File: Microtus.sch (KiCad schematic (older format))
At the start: 9 parts

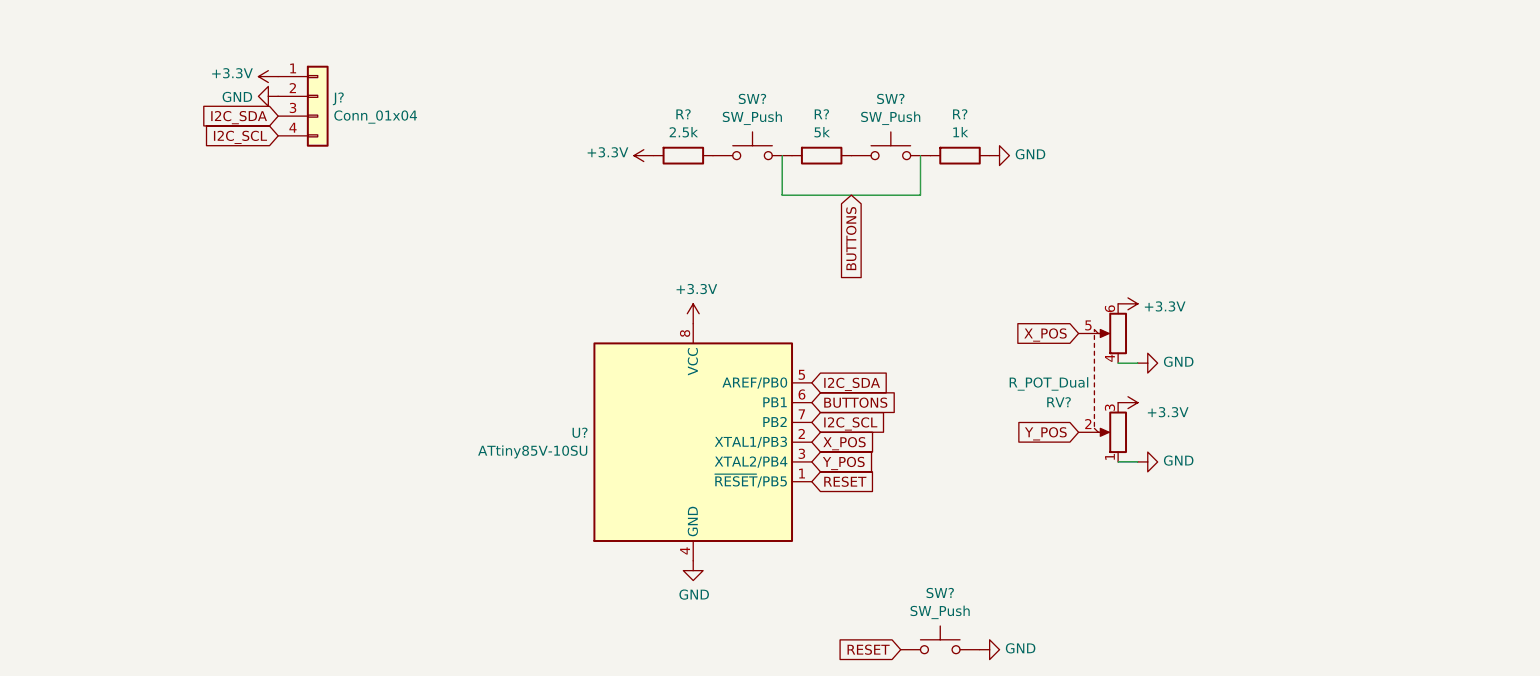
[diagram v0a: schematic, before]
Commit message: go with choc switches and 0805 SMDs
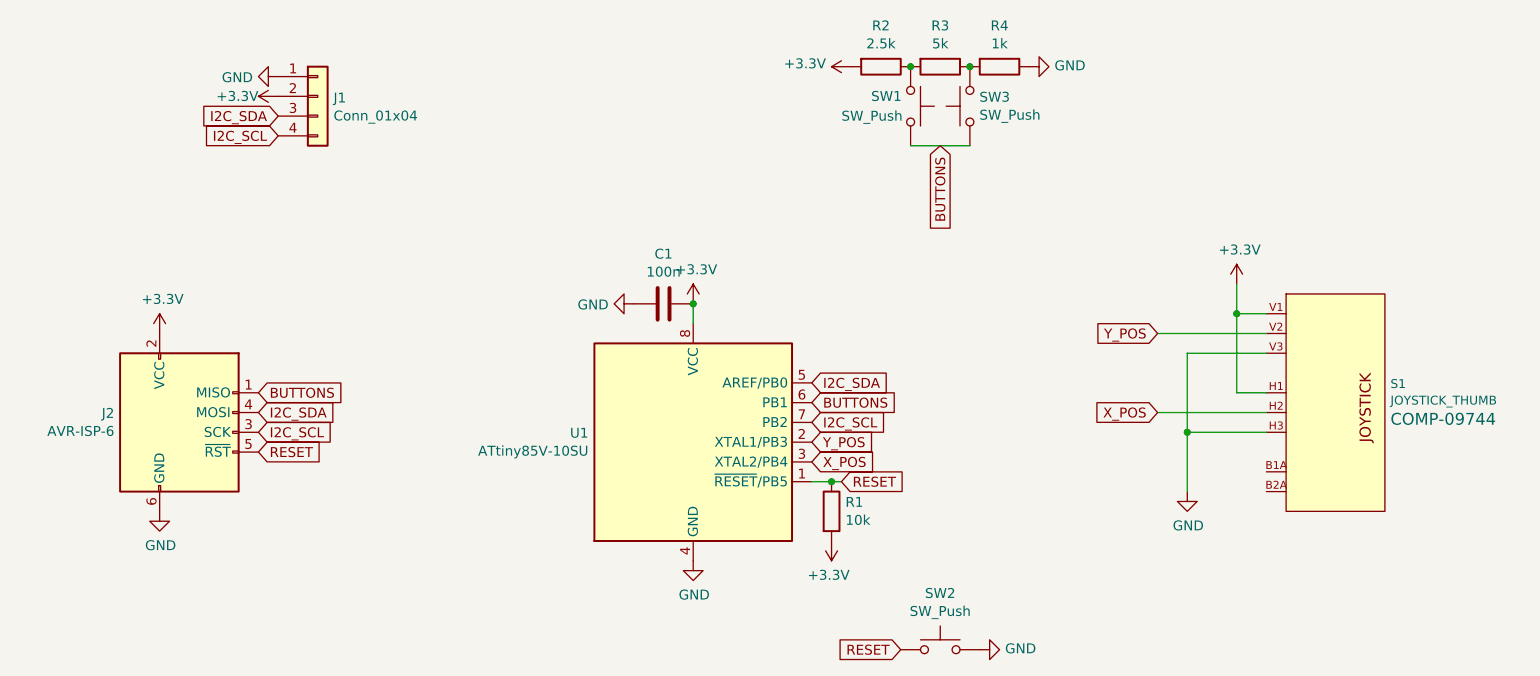
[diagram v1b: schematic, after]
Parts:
- removed RV?: R_POT_Dual, symbol Device:R_POT_Dual
- added C1: 100n, Capacitor_SMD:C_0805_2012Metric_Pad1.18x1.45mm_HandSolder, symbol Device:C
- added J2: AVR-ISP-6, Connector_PinHeader_1.00mm:PinHeader_2x03_P1.00mm_Vertical, symbol Connector:AVR-ISP-6
- added R1: 10k, Resistor_SMD:R_0805_2012Metric_Pad1.20x1.40mm_HandSolder, symbol Device:R
- added S1: JOYSTICK_THUMB, sparkfun-sw:JOYSTICK, symbol Sparkfun-sw:JOYSTICK_THUMB
- R2, R3, R4: renamed from R?; footprint Resistor_SMD:R_0603_1608Metric -> Resistor_SMD:R_0805_2012Metric_Pad1.20x1.40mm_HandSolder
- SW1, SW3: renamed from SW?; footprint Button_Switch_Keyboard:SW_Cherry_MX_1.00u_PCB -> Keebio:Kailh-PG1350-1u-NoLED
- SW2: renamed from SW?; footprint (none) -> Button_Switch_SMD:Panasonic_EVQPUL_EVQPUC
- gave numbers to parts that had none: 2
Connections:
- wire segments 5 -> 14
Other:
- moved on the sheet: R2, R3, R4, SW1, SW3

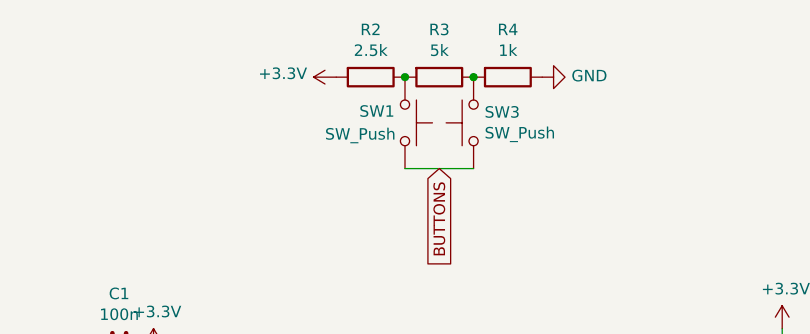
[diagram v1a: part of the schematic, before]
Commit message: Shrink and switch back to 0603
also round corners with 2mm radius
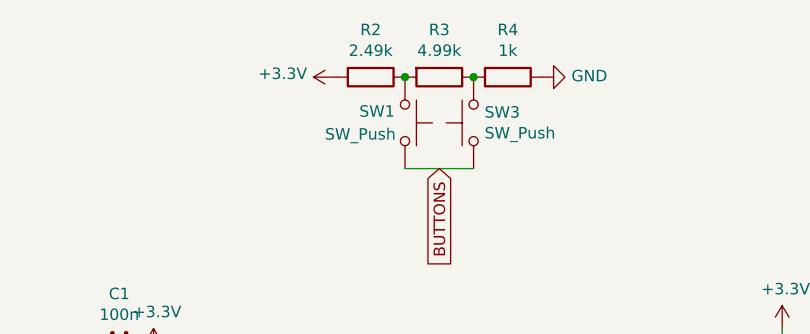
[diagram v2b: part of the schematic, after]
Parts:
- C1: footprint Capacitor_SMD:C_0805_2012Metric_Pad1.18x1.45mm_HandSolder -> Capacitor_SMD:C_0603_1608Metric; LCSC (none) -> C14663
- J2: footprint Connector_PinHeader_1.00mm:PinHeader_2x03_P1.00mm_Vertical -> Connector_PinHeader_2.54mm:PinHeader_2x03_P2.54mm_Vertical
- R1: footprint Resistor_SMD:R_0805_2012Metric_Pad1.20x1.40mm_HandSolder -> Resistor_SMD:R_0603_1608Metric; LCSC (none) -> C25804
- R2: value 2.5k -> 2.49k; footprint Resistor_SMD:R_0805_2012Metric_Pad1.20x1.40mm_HandSolder -> Resistor_SMD:R_0603_1608Metric; LCSC (none) -> C21189
- R3: value 5k -> 4.99k; footprint Resistor_SMD:R_0805_2012Metric_Pad1.20x1.40mm_HandSolder -> Resistor_SMD:R_0603_1608Metric; LCSC (none) -> C23046
- R4: footprint Resistor_SMD:R_0805_2012Metric_Pad1.20x1.40mm_HandSolder -> Resistor_SMD:R_0603_1608Metric; LCSC (none) -> C21189
- SW2: LCSC (none) -> C79174
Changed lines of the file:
@@
 P 6900 1750
 F 0 "R2" V 6693 1750 50  0000 C CNN
-F 1 "2.5k" V 6784 1750 50  0000 C CNN
-F 2 "Resistor_SMD:R_0805_2012Metric_Pad1.20x1.40mm_HandSolder" V 6830 1750 50  0001 C CNN
+F 1 "2.49k" V 6784 1750 50  0000 C CNN
+F 2 "Resistor_SMD:R_0603_1608Metric" V 6830 1750 50  0001 C CNN
 F 3 "~" H 6900 1750 50  0001 C CNN
+F 4 "C21189" H 6900 1750 50  0001 C CNN "LCSC"
 	1    6900 1750
 	0    1    1    0
@@
 P 7200 1750
 F 0 "R3" V 6993 1750 50  0000 C CNN
-F 1 "5k" V 7084 1750 50  0000 C CNN
-F 2 "Resistor_SMD:R_0805_2012Metric_Pad1.20x1.40mm_HandSolder" V 7130 1750 50  0001 C CNN
+F 1 "4.99k" V 7084 1750 50  0000 C CNN
+F 2 "Resistor_SMD:R_0603_1608Metric" V 7130 1750 50  0001 C CNN
 F 3 "~" H 7200 1750 50  0001 C CNN
+F 4 "C23046" H 7200 1750 50  0001 C CNN "LCSC"
 	1    7200 1750
 	0    1    1    0
@@
 F 0 "R4" V 7293 1750 50  0000 C CNN
 F 1 "1k" V 7384 1750 50  0000 C CNN
-F 2 "Resistor_SMD:R_0805_2012Metric_Pad1.20x1.40mm_HandSolder" V 7430 1750 50  0001 C CNN
+F 2 "Resistor_SMD:R_0603_1608Metric" V 7430 1750 50  0001 C CNN
 F 3 "~" H 7500 1750 50  0001 C CNN
+F 4 "C21189" H 7500 1750 50  0001 C CNN "LCSC"
 	1    7500 1750
 	0    1    1    0
@@
 F 2 "Button_Switch_SMD:Panasonic_EVQPUL_EVQPUC" H 7200 4900 50  0001 C CNN
 F 3 "~" H 7200 4900 50  0001 C CNN
+F 4 "C79174" H 7200 4700 50  0001 C CNN "LCSC"
 	1    7200 4700
 	1    0    0    -1
@@
 F 0 "C1" V 5548 2950 50  0000 C CNN
 F 1 "100n" V 5639 2950 50  0000 C CNN
-F 2 "Capacitor_SMD:C_0805_2012Metric_Pad1.18x1.45mm_HandSolder" H 5838 2800 50  0001 C CNN
+F 2 "Capacitor_SMD:C_0603_1608Metric" H 5838 2800 50  0001 C CNN
 F 3 "~" H 5800 2950 50  0001 C CNN
+F 4 "C14663" H 5800 2950 50  0001 C CNN "LCSC"
 	1    5800 2950
 	0    1    1    0
@@
 F 0 "R1" H 6720 4046 50  0000 L CNN
 F 1 "10k" H 6720 3955 50  0000 L CNN
-F 2 "Resistor_SMD:R_0805_2012Metric_Pad1.20x1.40mm_HandSolder" V 6580 4000 50  0001 C CNN
+F 2 "Resistor_SMD:R_0603_1608Metric" V 6580 4000 50  0001 C CNN
 F 3 "~" H 6650 4000 50  0001 C CNN
+F 4 "C25804" H 6650 4000 50  0001 C CNN "LCSC"
 	1    6650 4000
 	1    0    0    -1
@@
 F 0 "J2" H 3021 3696 50  0000 R CNN
 F 1 "AVR-ISP-6" H 3021 3605 50  0000 R CNN
-F 2 "Connector_PinHeader_1.00mm:PinHeader_2x03_P1.00mm_Vertical" V 3100 3650 50  0001 C CNN
+F 2 "Connector_PinHeader_2.54mm:PinHeader_2x03_P2.54mm_Vertical" V 3100 3650 50  0001 C CNN
 F 3 " ~" H 2075 3050 50  0001 C CNN
 	1    3350 3600
